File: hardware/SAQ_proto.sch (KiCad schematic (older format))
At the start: 40 parts, among them J1 Sense, J2 9V, J3 out, J4 SP, Q1 2N3904, SW1 SW_SPDT, U1 LM555, U2 LM386

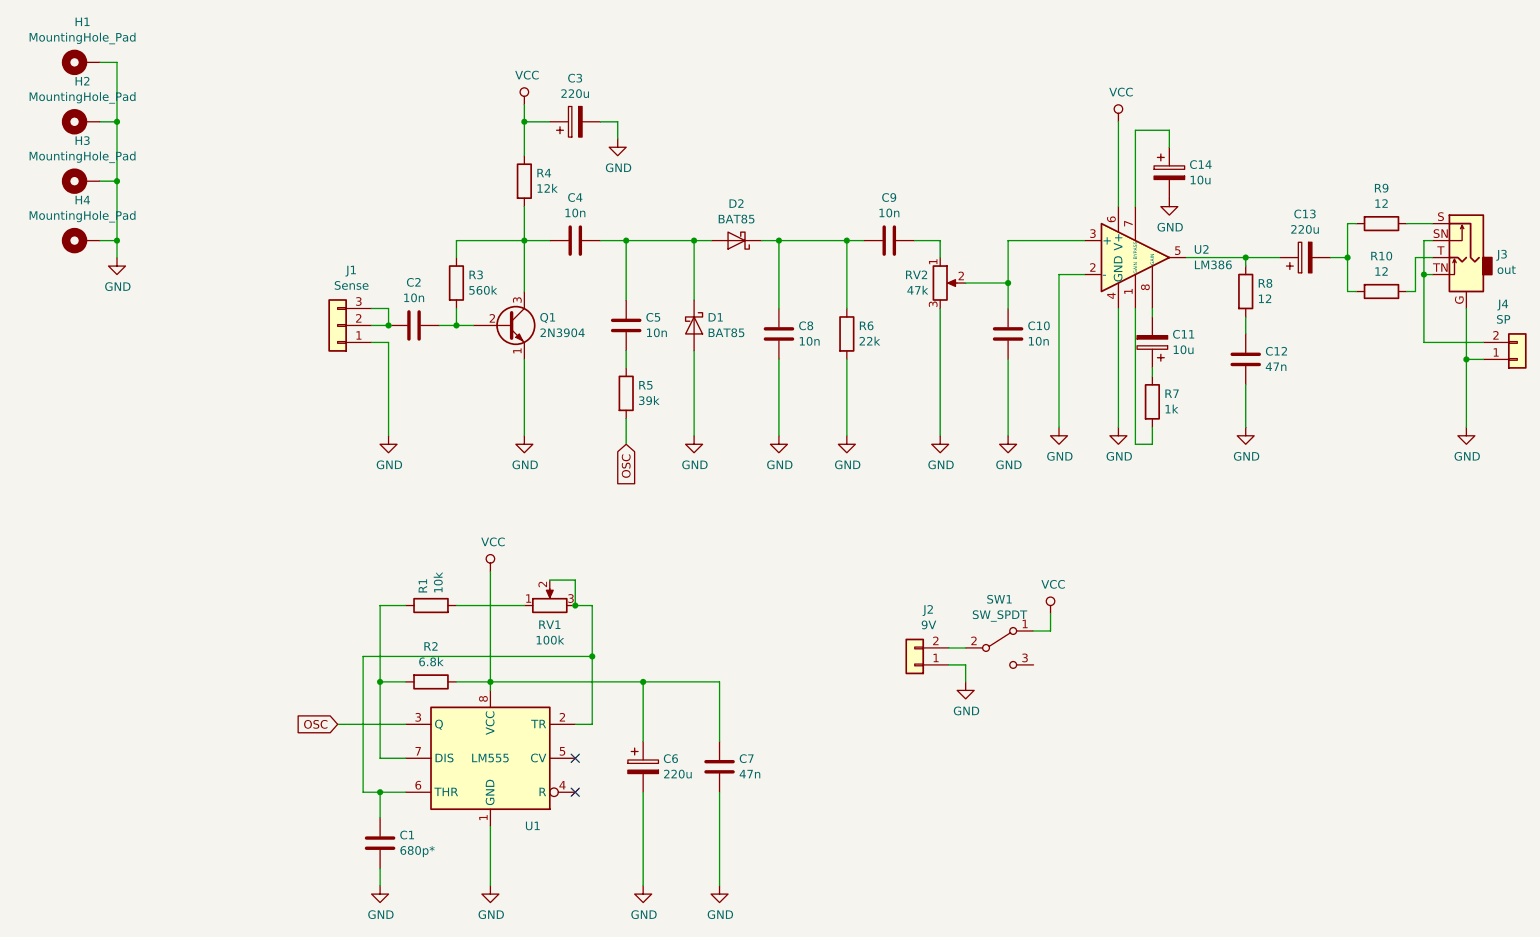
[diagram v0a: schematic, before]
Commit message: Added prototype circuit/board
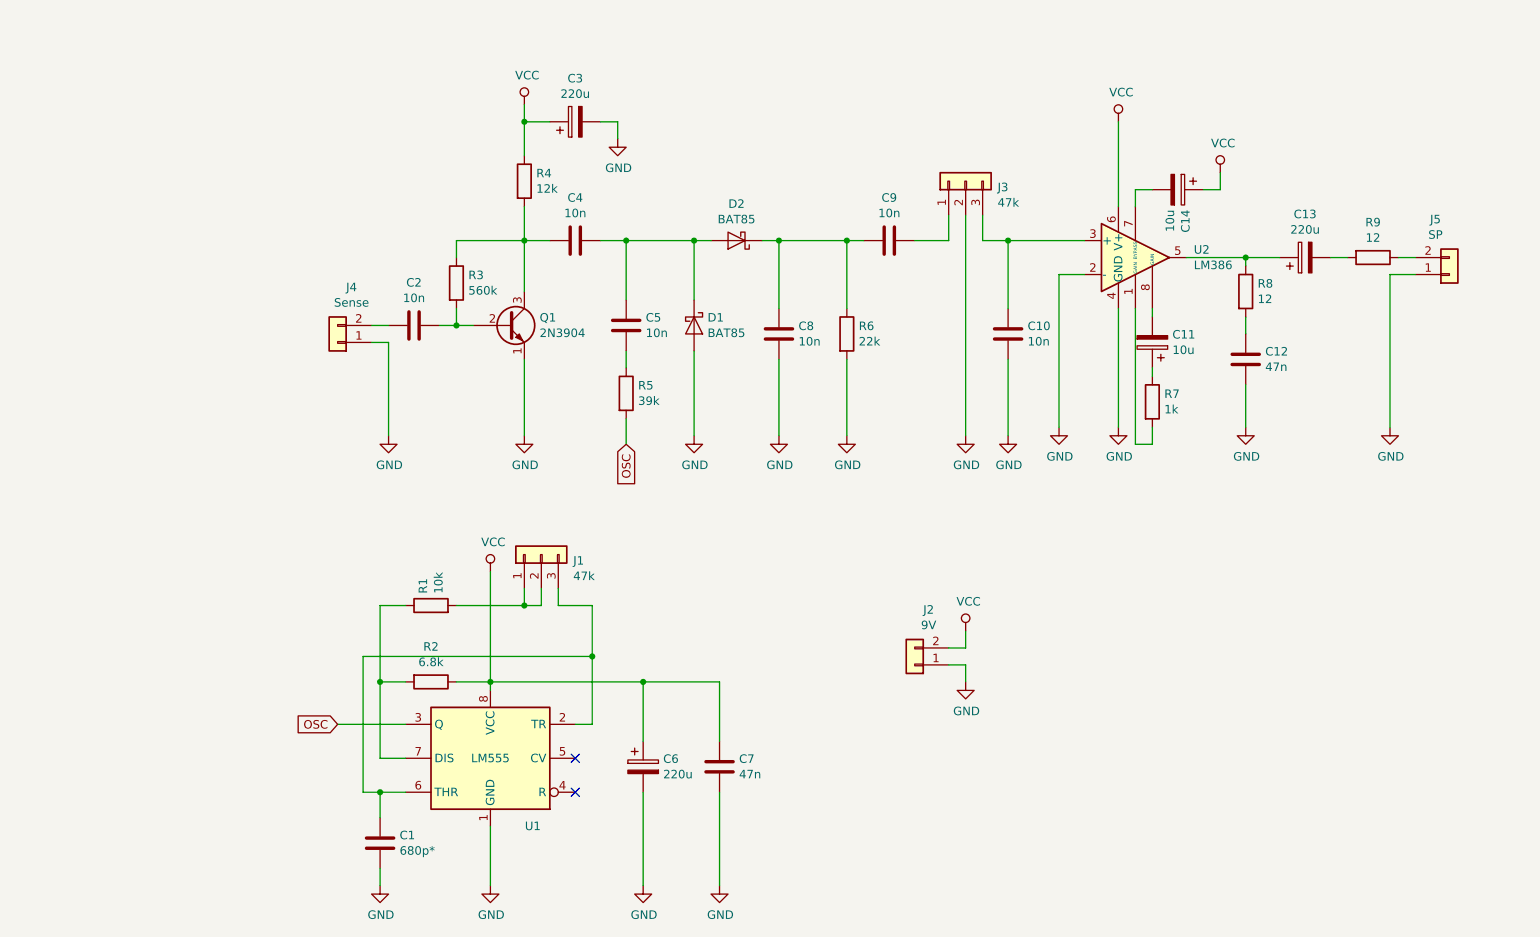
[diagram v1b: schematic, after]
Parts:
- removed H1, H2, H3, H4: MountingHole_Pad, MountingHole:MountingHole_3.2mm_M3_Pad_Via, symbol Mechanical:MountingHole_Pad
- removed J3: out, Connector_Audio:Jack_3.5mm_Ledino_KB3SPRS_Horizontal, symbol Connector:AudioJack2_Ground_Switch
- removed R10: 12, Resistor_THT:R_Axial_DIN0207_L6.3mm_D2.5mm_P2.54mm_Vertical, symbol Device:R
- removed RV1: 100k, Potentiometer_THT:Potentiometer_Alps_RK09K_Single_Vertical, symbol Device:R_POT
- removed RV2: 47k, Potentiometer_THT:Potentiometer_Alps_RK09K_Single_Vertical, symbol Device:R_POT
- removed SW1: SW_SPDT, Button_Switch_THT:SW_Slide_1P2T_CK_OS102011MS2Q, symbol Switch:SW_SPDT
- added J3: 47k, Connector_Molex:Molex_KK-254_AE-6410-03A_1x03_P2.54mm_Vertical, symbol Connector_Generic:Conn_01x03
- added J5: SP, Connector_Molex:Molex_KK-254_AE-6410-02A_1x02_P2.54mm_Vertical, symbol Connector_Generic:Conn_01x02
- C5, C8: footprint Capacitor_THT:C_Disc_D3.0mm_W2.0mm_P2.50mm -> Capacitor_THT:C_Disc_D4.3mm_W1.9mm_P5.00mm
- D1: footprint Diode_THT:D_DO-35_SOD27_P2.54mm_Vertical_AnodeUp -> Diode_THT:D_DO-35_SOD27_P5.08mm_Vertical_AnodeUp
- J1: value Sense -> 47k; footprint TerminalBlock_RND:TerminalBlock_RND_205-00013_1x03_P5.00mm_Horizontal -> Connector_Molex:Molex_KK-254_AE-6410-03A_1x03_P2.54mm_Vertical
- J4: value SP -> Sense
- R1: footprint Resistor_THT:R_Axial_DIN0207_L6.3mm_D2.5mm_P5.08mm_Vertical -> Resistor_THT:R_Axial_DIN0207_L6.3mm_D2.5mm_P2.54mm_Vertical
- R8, R9: footprint Resistor_THT:R_Axial_DIN0207_L6.3mm_D2.5mm_P2.54mm_Vertical -> Resistor_THT:R_Axial_DIN0207_L6.3mm_D2.5mm_P5.08mm_Vertical
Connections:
- net GND: now also J3.2 (Pin_2), J5.1 (Pin_1); no longer C14.2, J1.1 (Pin_1)
- net VCC: now also C14.1, J2.2 (Pin_2)
- net at C1.2, U1.2 (TR), U1.6 (THR): now also J1.3 (Pin_3)
- net at C9.2: now also J3.1 (Pin_1)
- net at C10.2, U2.3 (+): now also J3.3 (Pin_3)
- net at U2.7 (BYPASS): now also C14.2; no longer C14.1
- net at R9.1: now also J5.2 (Pin_2)
- net at R1.2: now also J1.1 (Pin_1), J1.2 (Pin_2)
- net at J4.2 (Pin_2): now also C2.2
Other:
- moved on the sheet: C14, J4, R9

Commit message: Fixed prototype.
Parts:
- J1: value 47k -> 100k
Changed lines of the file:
@@
 P 3850 4400
 F 0 "J1" V 3814 4212 50  0000 R CNN
-F 1 "47k" V 3723 4212 50  0000 R CNN
+F 1 "100k" V 3723 4212 50  0000 R CNN
 F 2 "Connector_Molex:Molex_KK-254_AE-6410-03A_1x03_P2.54mm_Vertical" H 3850 4400 50  0001 C CNN
 F 3 "~" H 3850 4400 50  0001 C CNN
